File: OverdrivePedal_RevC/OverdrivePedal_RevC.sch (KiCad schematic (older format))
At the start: 26 parts, among them J1 AudioJack2-Connector, J2 Barrel_Jack, J3 Conn_01x05, J4 SW_SPST, J6 AudioJack2-Connector, U1 DG468DV_T1_E3, U2 TL071, U4 DG468DV_T1_E3, U5 STM32L011D4Px, U6 DG468DV_T1_E3

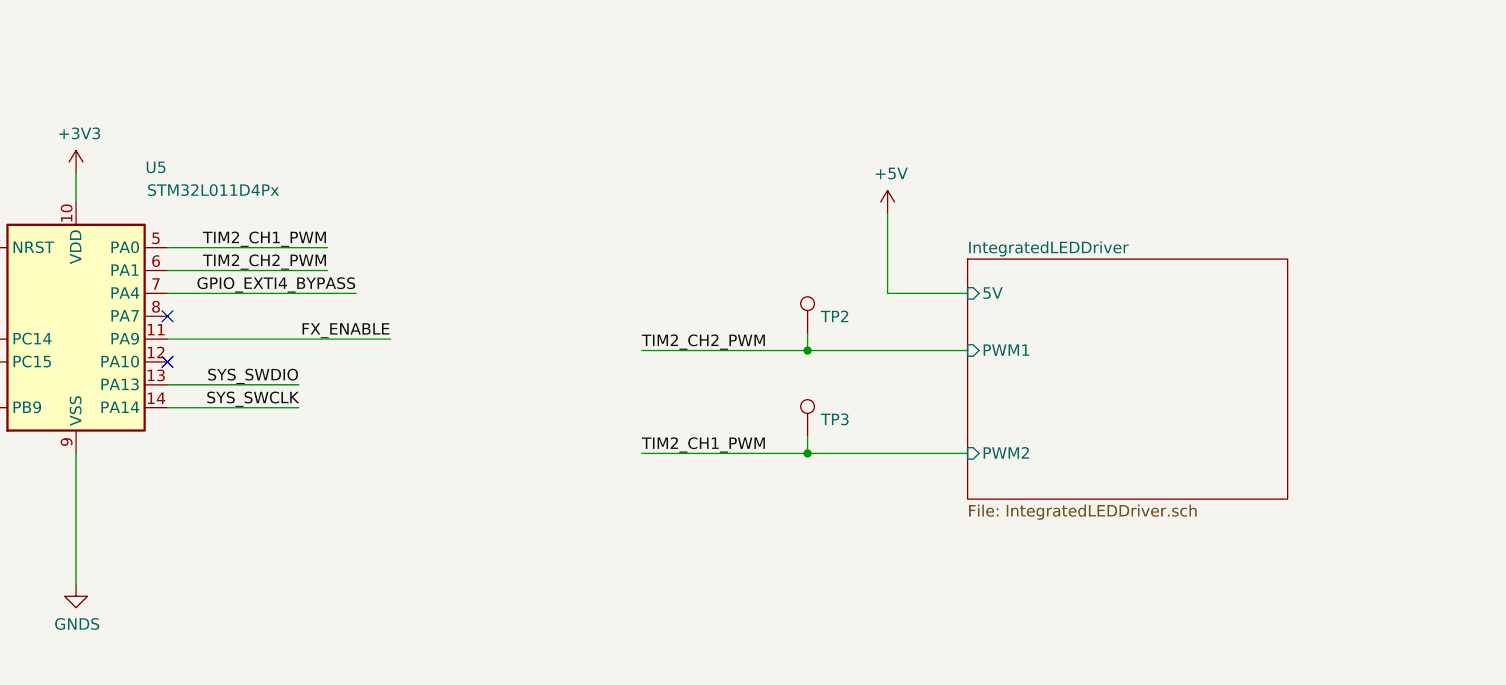
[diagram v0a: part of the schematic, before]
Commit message: updated revc
- Changed ICP header from 2.54 to 1.27
- Added trim pot connected to ADC IN7 (PA7)
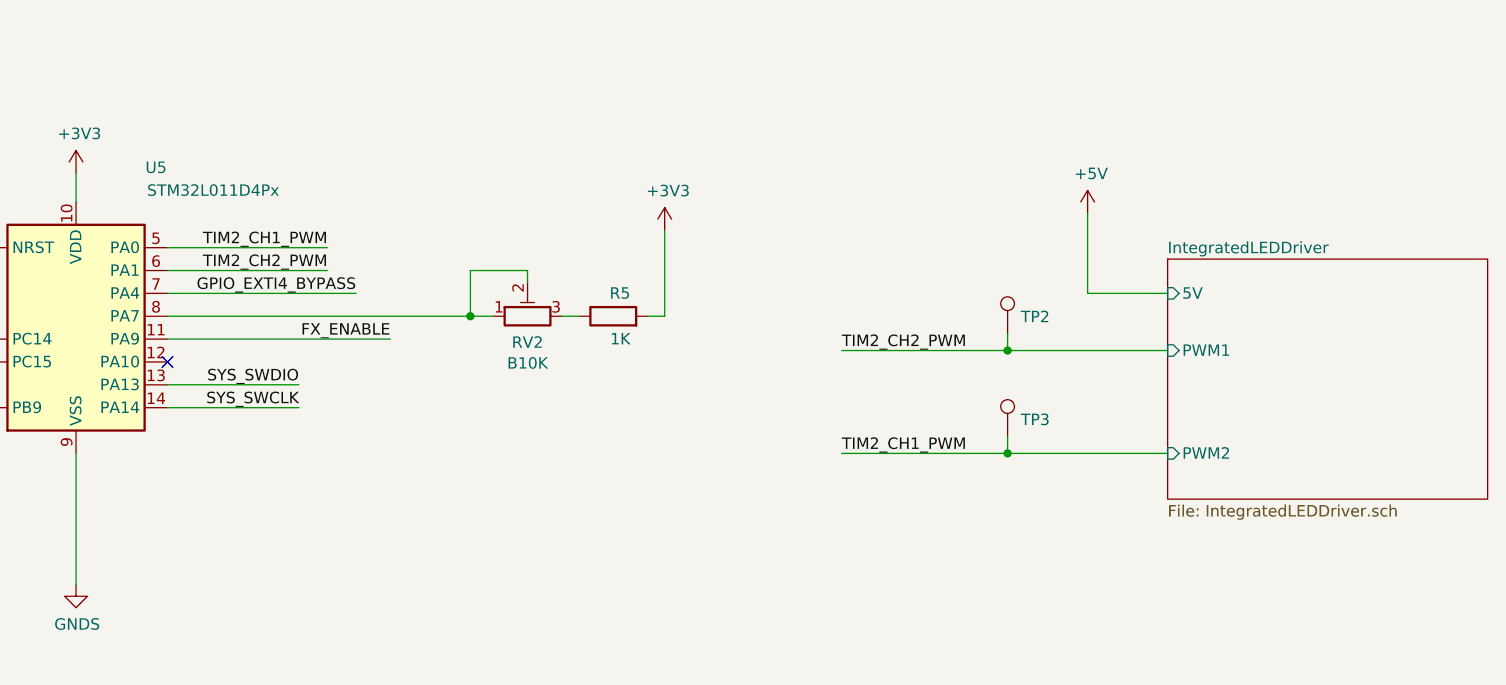
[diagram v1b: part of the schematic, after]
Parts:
- added R5: 1K, Resistor_SMD:R_0402_1005Metric, symbol Device:R
- added RV2: B10K, Potentiometer_THT:Potentiometer_Vishay_T73XW_Horizontal, symbol Device:R_POT_TRIM
- J3: footprint Connector_PinSocket_2.54mm:PinSocket_1x05_P2.54mm_Vertical -> Connector_PinHeader_1.27mm:PinHeader_1x05_P1.27mm_Vertical
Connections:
- net +3V3: now also R5.2
- net at U5.8 (PA7): now also RV2.1, RV2.2
- new net: R5.1, RV2.3
- no-connect marks 5 -> 4
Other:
- moved on the sheet: TP2, TP3
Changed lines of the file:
@@
 F 0 "J3" H 8775 10725 50  0000 L CNN
 F 1 "Conn_01x05" H 8650 10625 50  0000 L CNN
-F 2 "Connector_PinSocket_2.54mm:PinSocket_1x05_P2.54mm_Vertical" H 8950 10250 50  0001 C CNN
+F 2 "Connector_PinHeader_1.27mm:PinHeader_1x05_P1.27mm_Vertical" H 8950 10250 50  0001 C CNN
 F 3 "~" H 8950 10250 50  0001 C CNN
 	1    8950 10250
@@
 	4600 3250 5625 3250
 $Sheet
-S 12500 7125 1400 1050
+S 13375 7125 1400 1050
 U 5EA2BA44
 F0 "IntegratedLEDDriver" 50
 F1 "IntegratedLEDDriver.sch" 50
-F2 "PWM1" I L 12500 7525 50
-F3 "5V" I L 12500 7275 50
-F4 "PWM2" I L 12500 7975 50
+F2 "PWM1" I L 13375 7525 50
+F3 "5V" I L 13375 7275 50
+F4 "PWM2" I L 13375 7975 50
 $EndSheet
 Wire Wire Line
-	12500 7525 11800 7525
-Wire Wire Line
-	12500 7975 11800 7975
-Text Label 11075 7975 0    50   ~ 0
+	13375 7525 12675 7525
+Wire Wire Line
+	13375 7975 12675 7975
+Text Label 11950 7975 0    50   ~ 0
 TIM2_CH1_PWM
-Text Label 11075 7525 0    50   ~ 0
+Text Label 11950 7525 0    50   ~ 0
 TIM2_CH2_PWM
 Wire Wire Line
-	12500 7275 12150 7275
-Wire Wire Line
-	12150 7275 12150 6925
+	13375 7275 13025 7275
+Wire Wire Line
+	13025 7275 13025 6925
 $Comp
 L power:+5V #PWR0108
 U 1 1 5EAA956B
-P 12150 6925
-F 0 "#PWR0108" H 12150 6775 50  0001 C CNN
-F 1 "+5V" H 12165 7098 50  0000 C CNN
-F 2 "" H 12150 6925 50  0001 C CNN
-F 3 "" H 12150 6925 50  0001 C CNN
-	1    12150 6925
+P 13025 6925
+F 0 "#PWR0108" H 13025 6775 50  0001 C CNN
+F 1 "+5V" H 13040 7098 50  0000 C CNN
+F 2 "" H 13025 6925 50  0001 C CNN
+F 3 "" H 13025 6925 50  0001 C CNN
+	1    13025 6925
 	1    0    0    -1
 $EndComp
@@
 L Connector:TestPoint TP?
 U 1 1 5E84562F
-P 11800 7900
+P 12675 7900
 AR Path="/5E6165F4/5E84562F" Ref="TP?"  Part="1"
 AR Path="/5E84562F" Ref="TP3"  Part="1"
-F 0 "TP3" H 11858 7972 50  0000 L CNN
-F 1 "TestPoint" H 11858 7927 50  0001 L CNN
-F 2 "TestPoint:TestPoint_Pad_1.0x1.0mm" H 12000 7900 50  0001 C CNN
-F 3 "~" H 12000 7900 50  0001 C CNN
-	1    11800 7900
+F 0 "TP3" H 12733 7972 50  0000 L CNN
+F 1 "TestPoint" H 12733 7927 50  0001 L CNN
+F 2 "TestPoint:TestPoint_Pad_1.0x1.0mm" H 12875 7900 50  0001 C CNN
+F 3 "~" H 12875 7900 50  0001 C CNN
+	1    12675 7900
 	1    0    0    -1
 $EndComp
@@
 L Connector:TestPoint TP?
 U 1 1 5E848751
-P 11800 7450
+P 12675 7450
 AR Path="/5E6165F4/5E848751" Ref="TP?"  Part="1"
 AR Path="/5E848751" Ref="TP2"  Part="1"
-F 0 "TP2" H 11858 7522 50  0000 L CNN
-F 1 "TestPoint" H 11858 7477 50  0001 L CNN
-F 2 "TestPoint:TestPoint_Pad_1.0x1.0mm" H 12000 7450 50  0001 C CNN
-F 3 "~" H 12000 7450 50  0001 C CNN
-	1    11800 7450
-	1    0    0    -1
-$EndComp
-Wire Wire Line
-	11800 7450 11800 7525
-Connection ~ 11800 7525
-Wire Wire Line
-	11800 7525 11075 7525
-Wire Wire Line
-	11800 7900 11800 7975
-Connection ~ 11800 7975
-Wire Wire Line
-	11800 7975 11075 7975
+F 0 "TP2" H 12733 7522 50  0000 L CNN
+F 1 "TestPoint" H 12733 7477 50  0001 L CNN
+F 2 "TestPoint:TestPoint_Pad_1.0x1.0mm" H 12875 7450 50  0001 C CNN
+F 3 "~" H 12875 7450 50  0001 C CNN
+	1    12675 7450
+	1    0    0    -1
+$EndComp
+Wire Wire Line
+	12675 7450 12675 7525
+Connection ~ 12675 7525
+Wire Wire Line
+	12675 7525 11950 7525
+Wire Wire Line
+	12675 7900 12675 7975
+Connection ~ 12675 7975
+Wire Wire Line
+	12675 7975 11950 7975
 Wire Wire Line
 	8200 7475 7225 7475
@@
 DNF
 NoConn ~ 8200 7575
-NoConn ~ 9000 7375
 NoConn ~ 9000 7575
 Text Notes 7225 7600 0    50   ~ 0
@@
 	1    0    0    -1
 $EndComp
+$Comp
+L Device:R_POT_TRIM RV2
+U 1 1 5E9406BD
+P 10575 7375
+F 0 "RV2" V 10460 7375 50  0000 C CNN
+F 1 "B10K" V 10369 7375 50  0000 C CNN
+F 2 "Potentiometer_THT:Potentiometer_Vishay_T73XW_Horizontal" H 10575 7375 50  0001 C CNN
+F 3 "~" H 10575 7375 50  0001 C CNN
+	1    10575 7375
+	0    -1   -1   0
+$EndComp
+Wire Wire Line
+	9000 7375 10325 7375
+Wire Wire Line
+	10575 7225 10575 7175
+Wire Wire Line
+	10575 7175 10325 7175
+Wire Wire Line
+	10325 7175 10325 7375
+Connection ~ 10325 7375
+Wire Wire Line
+	10325 7375 10425 7375
+Wire Wire Line
+	10725 7375 10800 7375
+Wire Wire Line
+	11175 7375 11175 7000
+$Comp
+L power:+3V3 #PWR07
+U 1 1 5E94D61E
+P 11175 7000
+F 0 "#PWR07" H 11175 6850 50  0001 C CNN
+F 1 "+3V3" H 11190 7173 50  0000 C CNN
+F 2 "" H 11175 7000 50  0001 C CNN
+F 3 "" H 11175 7000 50  0001 C CNN
+	1    11175 7000
+	1    0    0    -1
+$EndComp
+$Comp
+L Device:R R5
+U 1 1 5E95B0C7
+P 10950 7375
+F 0 "R5" V 11050 7300 50  0000 L CNN
+F 1 "1K" V 10850 7300 50  0000 L CNN
+F 2 "Resistor_SMD:R_0402_1005Metric" V 10880 7375 50  0001 C CNN
+F 3 "~" H 10950 7375 50  0001 C CNN
+	1    10950 7375
+	0    -1   -1   0
+$EndComp
+Wire Wire Line
+	11100 7375 11175 7375
 $EndSCHEMATC

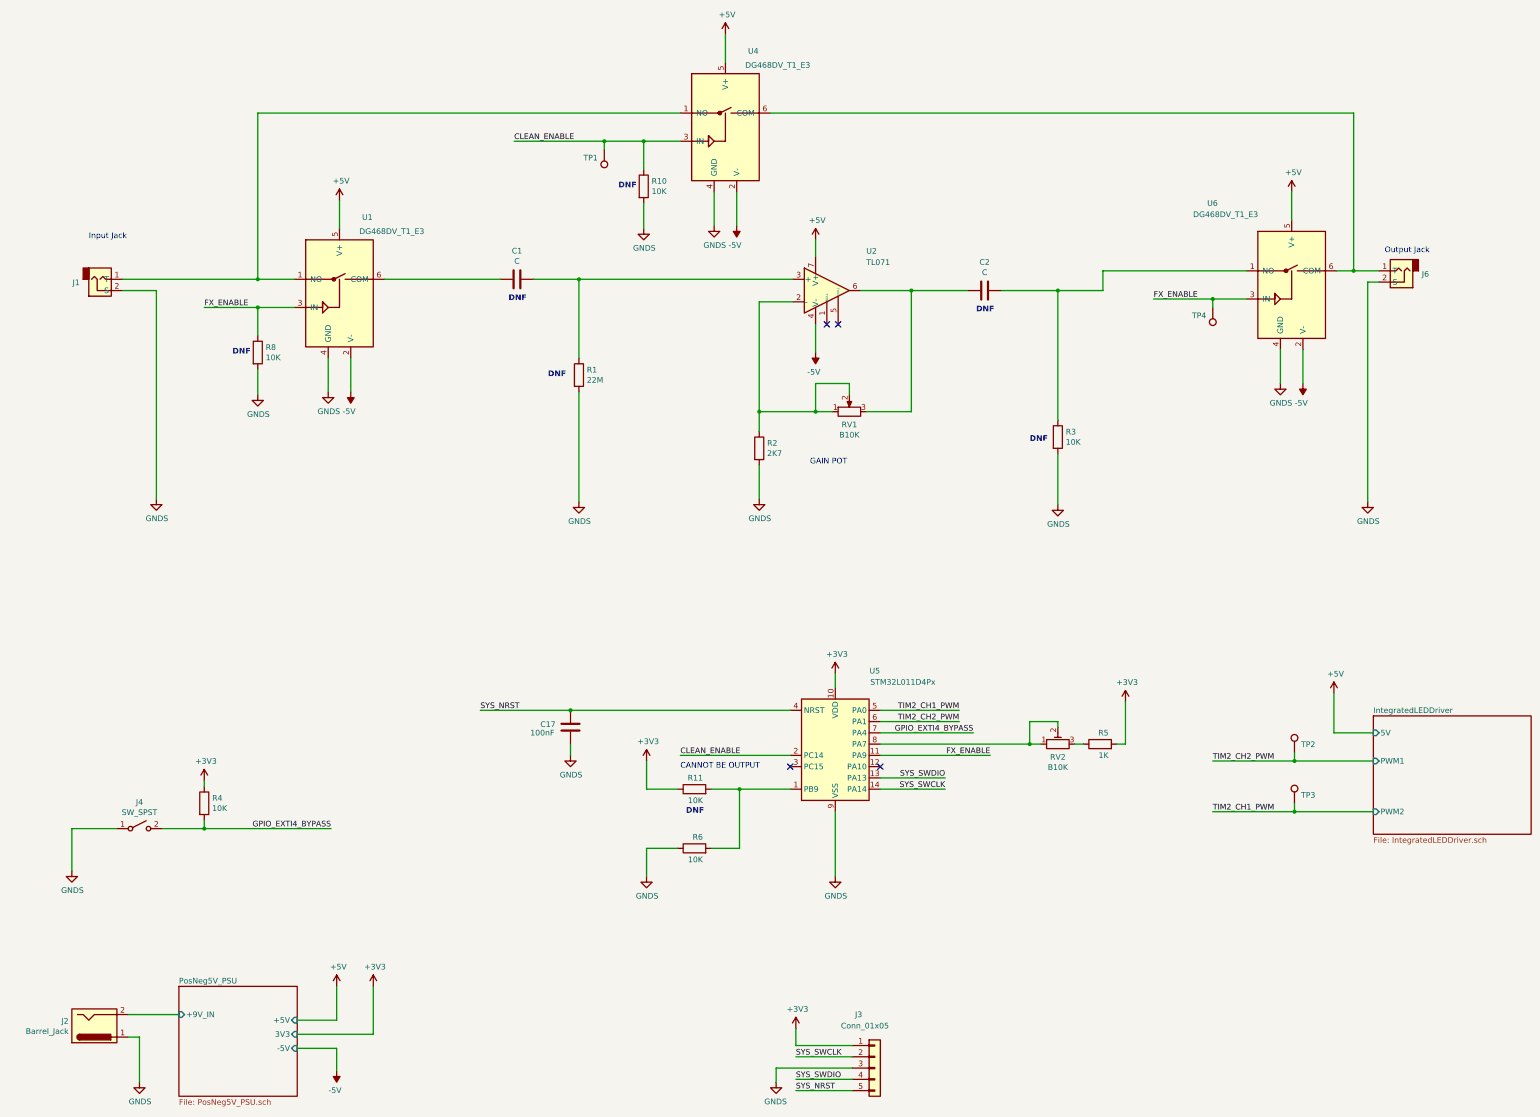
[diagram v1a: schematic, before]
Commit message: fixed wiring mistake on trim pot
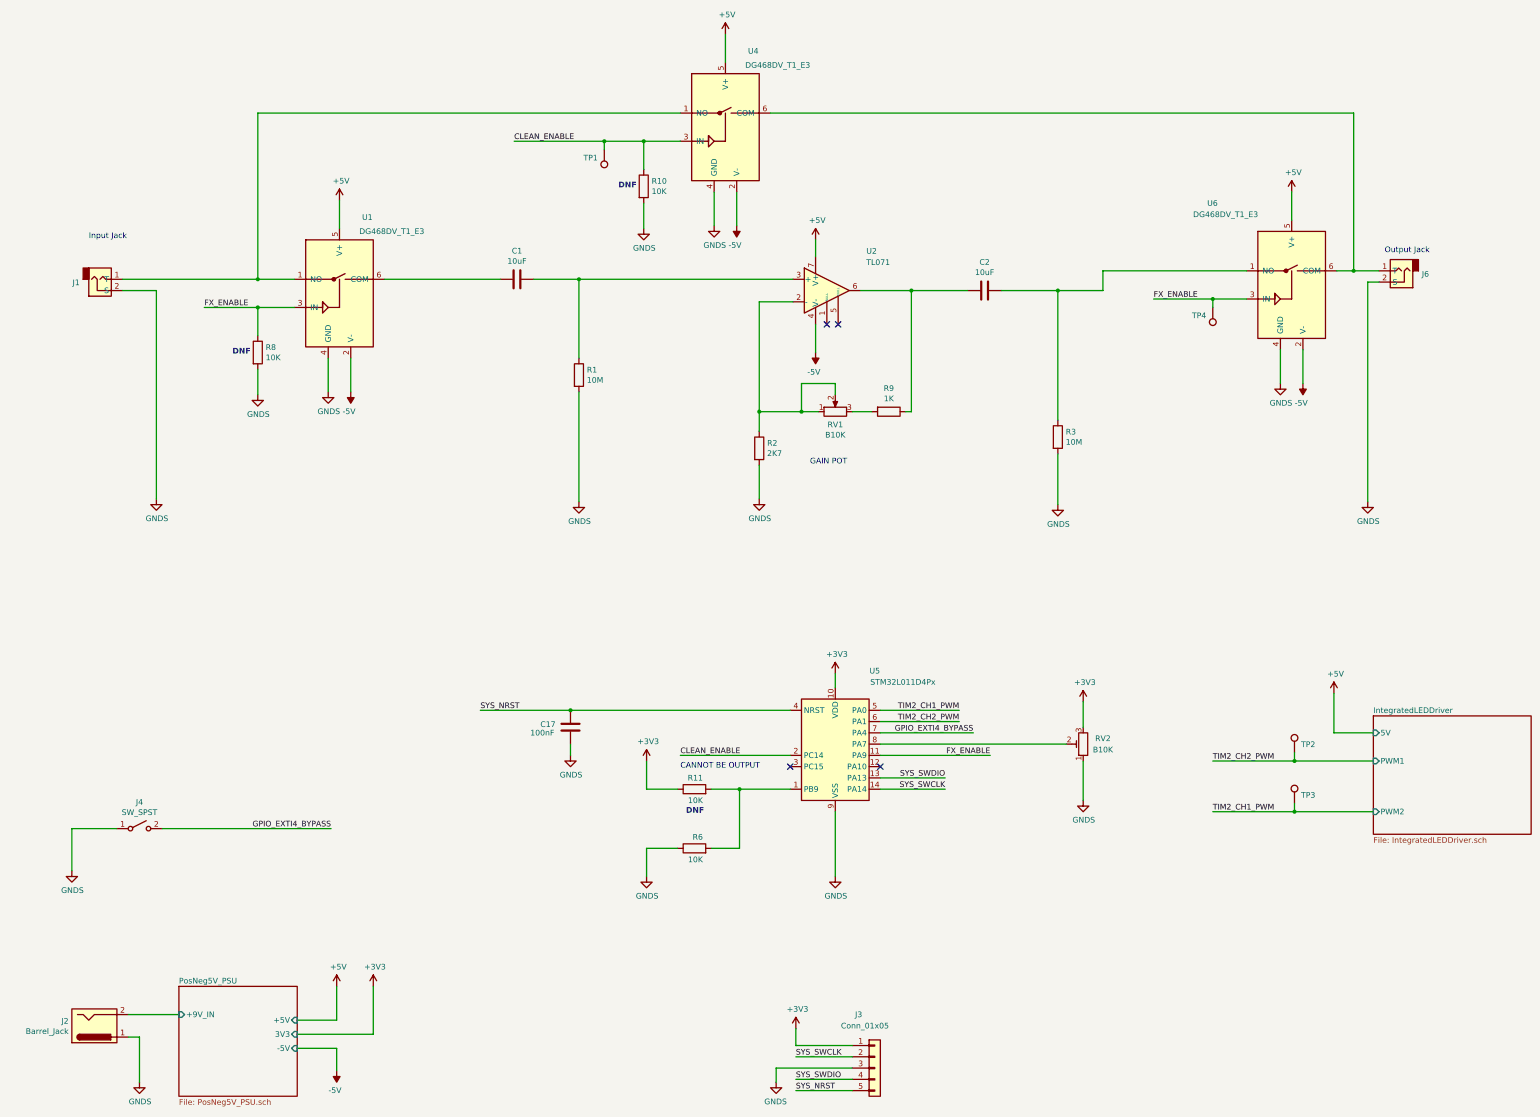
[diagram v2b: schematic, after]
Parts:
- removed R4: 10K, Resistor_SMD:R_0402_1005Metric, symbol Device:R
- removed R5: 1K, Resistor_SMD:R_0402_1005Metric, symbol Device:R
- added R9: 1K, Resistor_SMD:R_0402_1005Metric, symbol Device:R
- C1, C2: value C -> 10uF
- R1: value 22M -> 10M
- R3: value 10K -> 10M
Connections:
- net +3V3: now also RV2.3
- net GNDS: now also RV2.1
- net at C2.2, U2.6: now also R9.1; no longer RV1.3
- net at RV2.2, U5.8 (PA7): no longer RV2.1
- new net: R9.2, RV1.3
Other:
- moved on the sheet: RV1, RV2
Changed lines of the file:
@@
 	9275 3350 8825 3350
 Wire Wire Line
-	8725 4275 8725 4175
-Wire Wire Line
-	8725 4175 8425 4175
+	8600 4275 8600 4175
+Wire Wire Line
+	8600 4175 8300 4175
 $Comp
 L Device:R R2
@@
 P 10575 4650
 F 0 "R3" H 10645 4696 50  0000 L CNN
-F 1 "10K" H 10645 4605 50  0000 L CNN
+F 1 "10M" H 10645 4605 50  0000 L CNN
 F 2 "Resistor_SMD:R_0402_1005Metric" V 10505 4650 50  0001 C CNN
 F 3 "~" H 10575 4650 50  0001 C CNN
@@
 P 6325 4100
 F 0 "R1" H 6395 4146 50  0000 L CNN
-F 1 "22M" H 6395 4055 50  0000 L CNN
+F 1 "10M" H 6395 4055 50  0000 L CNN
 F 2 "Resistor_SMD:R_0402_1005Metric" V 6255 4100 50  0001 C CNN
 F 3 "~" H 6325 4100 50  0001 C CNN
@@
 P 9925 3350
 F 0 "C2" V 9673 3350 50  0000 C CNN
-F 1 "C" V 9764 3350 50  0000 C CNN
+F 1 "10uF" V 9764 3350 50  0000 C CNN
 F 2 "Capacitor_SMD:C_0402_1005Metric" H 9963 3200 50  0001 C CNN
 F 3 "~" H 9925 3350 50  0001 C CNN
@@
 P 5775 3250
 F 0 "C1" V 5523 3250 50  0000 C CNN
-F 1 "C" V 5614 3250 50  0000 C CNN
+F 1 "10uF" V 5614 3250 50  0000 C CNN
 F 2 "Capacitor_SMD:C_0402_1005Metric" H 5813 3100 50  0001 C CNN
 F 3 "~" H 5775 3250 50  0001 C CNN
@@
 L Device:R_POT RV1
 U 1 1 5EF6924D
-P 8725 4425
-F 0 "RV1" V 8610 4425 50  0000 C CNN
-F 1 "B10K" V 8519 4425 50  0000 C CNN
-F 2 "Connector_PinHeader_2.54mm:PinHeader_1x03_P2.54mm_Vertical" H 8725 4425 50  0001 C CNN
-F 3 "~" H 8725 4425 50  0001 C CNN
-	1    8725 4425
+P 8600 4425
+F 0 "RV1" V 8485 4425 50  0000 C CNN
+F 1 "B10K" V 8394 4425 50  0000 C CNN
+F 2 "Connector_PinHeader_2.54mm:PinHeader_1x03_P2.54mm_Vertical" H 8600 4425 50  0001 C CNN
+F 3 "~" H 8600 4425 50  0001 C CNN
+	1    8600 4425
 	0    -1   -1   0
 $EndComp
 Wire Wire Line
-	8425 4425 8575 4425
-Wire Wire Line
-	8425 4175 8425 4425
-Wire Wire Line
-	8425 4425 7925 4425
-Connection ~ 8425 4425
+	8300 4425 8450 4425
+Wire Wire Line
+	8300 4175 8300 4425
+Wire Wire Line
+	8300 4425 7925 4425
+Connection ~ 8300 4425
 Connection ~ 7925 4425
 Wire Wire Line
 	9275 3350 9275 4425
 Wire Wire Line
-	8875 4425 9275 4425
+	8750 4425 8925 4425
 Wire Wire Line
 	7925 3450 7925 4425
@@
 Wire Wire Line
 	2225 8125 1825 8125
-Wire Wire Line
-	2625 8125 3000 8125
-Wire Wire Line
-	3000 8125 3000 8050
-$Comp
-L power:+3V3 #PWR016
-U 1 1 5F149284
-P 3000 7700
-F 0 "#PWR016" H 3000 7550 50  0001 C CNN
-F 1 "+3V3" H 3015 7873 50  0000 C CNN
-F 2 "" H 3000 7700 50  0001 C CNN
-F 3 "" H 3000 7700 50  0001 C CNN
-	1    3000 7700
-	1    0    0    -1
-$EndComp
-$Comp
-L Device:R R4
-U 1 1 5F149794
-P 3000 7900
-F 0 "R4" H 3070 7946 50  0000 L CNN
-F 1 "10K" H 3070 7855 50  0000 L CNN
-F 2 "Resistor_SMD:R_0402_1005Metric" V 2930 7900 50  0001 C CNN
-F 3 "~" H 3000 7900 50  0001 C CNN
-	1    3000 7900
-	1    0    0    -1
-$EndComp
-Wire Wire Line
-	3000 7750 3000 7700
-Wire Wire Line
-	3000 8125 4125 8125
-Connection ~ 3000 8125
 Text Label 4125 8125 2    50   ~ 0
 GPIO_EXTI4_BYPASS
@@
 	-1   0    0    1
 $EndComp
-Text Notes 9850 3550 0    50   ~ 10
-DNF
-Text Notes 5700 3450 0    50   ~ 10
-DNF
-Text Notes 6050 4125 0    50   ~ 10
-DNF
-Text Notes 10325 4700 0    50   ~ 10
-DNF
 $Comp
 L Device:R R10
@@
 	1    0    0    -1
 $EndComp
+Wire Wire Line
+	10800 7225 10800 7000
+$Comp
+L power:+3V3 #PWR07
+U 1 1 5E94D61E
+P 10800 7000
+F 0 "#PWR07" H 10800 6850 50  0001 C CNN
+F 1 "+3V3" H 10815 7173 50  0000 C CNN
+F 2 "" H 10800 7000 50  0001 C CNN
+F 3 "" H 10800 7000 50  0001 C CNN
+	1    10800 7000
+	1    0    0    -1
+$EndComp
+$Comp
+L Device:R R9
+U 1 1 5EA072DE
+P 9075 4425
+F 0 "R9" V 8868 4425 50  0000 C CNN
+F 1 "1K" V 8959 4425 50  0000 C CNN
+F 2 "Resistor_SMD:R_0402_1005Metric" V 9005 4425 50  0001 C CNN
+F 3 "~" H 9075 4425 50  0001 C CNN
+	1    9075 4425
+	0    1    1    0
+$EndComp
+Wire Wire Line
+	9225 4425 9275 4425
 $Comp
 L Device:R_POT_TRIM RV2
 U 1 1 5E9406BD
-P 10575 7375
-F 0 "RV2" V 10460 7375 50  0000 C CNN
-F 1 "B10K" V 10369 7375 50  0000 C CNN
-F 2 "Potentiometer_THT:Potentiometer_Vishay_T73XW_Horizontal" H 10575 7375 50  0001 C CNN
-F 3 "~" H 10575 7375 50  0001 C CNN
-	1    10575 7375
-	0    -1   -1   0
-$EndComp
-Wire Wire Line
-	9000 7375 10325 7375
-Wire Wire Line
-	10575 7225 10575 7175
-Wire Wire Line
-	10575 7175 10325 7175
-Wire Wire Line
-	10325 7175 10325 7375
-Connection ~ 10325 7375
-Wire Wire Line
-	10325 7375 10425 7375
-Wire Wire Line
-	10725 7375 10800 7375
-Wire Wire Line
-	11175 7375 11175 7000
-$Comp
-L power:+3V3 #PWR07
-U 1 1 5E94D61E
-P 11175 7000
-F 0 "#PWR07" H 11175 6850 50  0001 C CNN
-F 1 "+3V3" H 11190 7173 50  0000 C CNN
-F 2 "" H 11175 7000 50  0001 C CNN
-F 3 "" H 11175 7000 50  0001 C CNN
-	1    11175 7000
-	1    0    0    -1
-$EndComp
-$Comp
-L Device:R R5
-U 1 1 5E95B0C7
-P 10950 7375
-F 0 "R5" V 11050 7300 50  0000 L CNN
-F 1 "1K" V 10850 7300 50  0000 L CNN
-F 2 "Resistor_SMD:R_0402_1005Metric" V 10880 7375 50  0001 C CNN
-F 3 "~" H 10950 7375 50  0001 C CNN
-	1    10950 7375
-	0    -1   -1   0
-$EndComp
-Wire Wire Line
-	11100 7375 11175 7375
+P 10800 7375
+F 0 "RV2" H 10625 7325 50  0000 C CNN
+F 1 "B10K" H 10625 7425 50  0000 C CNN
+F 2 "Potentiometer_THT:Potentiometer_Vishay_T73XW_Horizontal" H 10800 7375 50  0001 C CNN
+F 3 "~" H 10800 7375 50  0001 C CNN
+	1    10800 7375
+	-1   0    0    1
+$EndComp
+Wire Wire Line
+	9000 7375 10650 7375
+Wire Wire Line
+	10800 7525 10800 7875
+$Comp
+L power:GNDS #PWR0112
+U 1 1 5EA208A0
+P 10800 7875
+F 0 "#PWR0112" H 10800 7625 50  0001 C CNN
+F 1 "GNDS" H 10805 7702 50  0000 C CNN
+F 2 "" H 10800 7875 50  0001 C CNN
+F 3 "" H 10800 7875 50  0001 C CNN
+	1    10800 7875
+	1    0    0    -1
+$EndComp
+Wire Wire Line
+	2625 8125 4125 8125
 $EndSCHEMATC
